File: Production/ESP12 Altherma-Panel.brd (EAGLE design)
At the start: 80.1 x 49.8 mm, 53 parts, among them CON1 PGM/BT Serial, CON2 X85A - PL, CON3 X10A, CON5 Thermo Rly, K1 HRS1KH-S_DC5V, K2 HRS1KH-S_DC5V, U1 TLP291-4, U2 AP2112K-3.3, U4 DRDC3105E6-7, U5 SN74LVC1G125GV

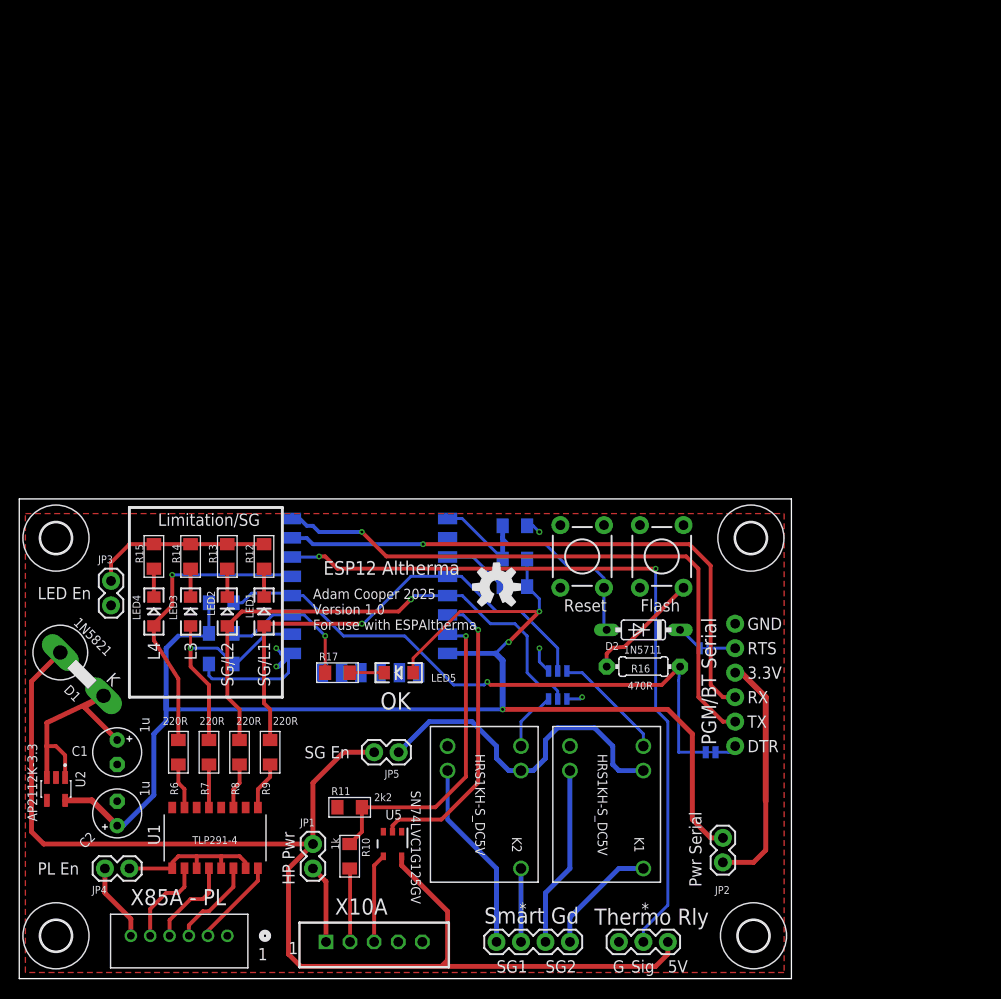
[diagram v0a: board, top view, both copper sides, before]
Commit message: Added layers 125/6 in BRD. Added panelised BRD.
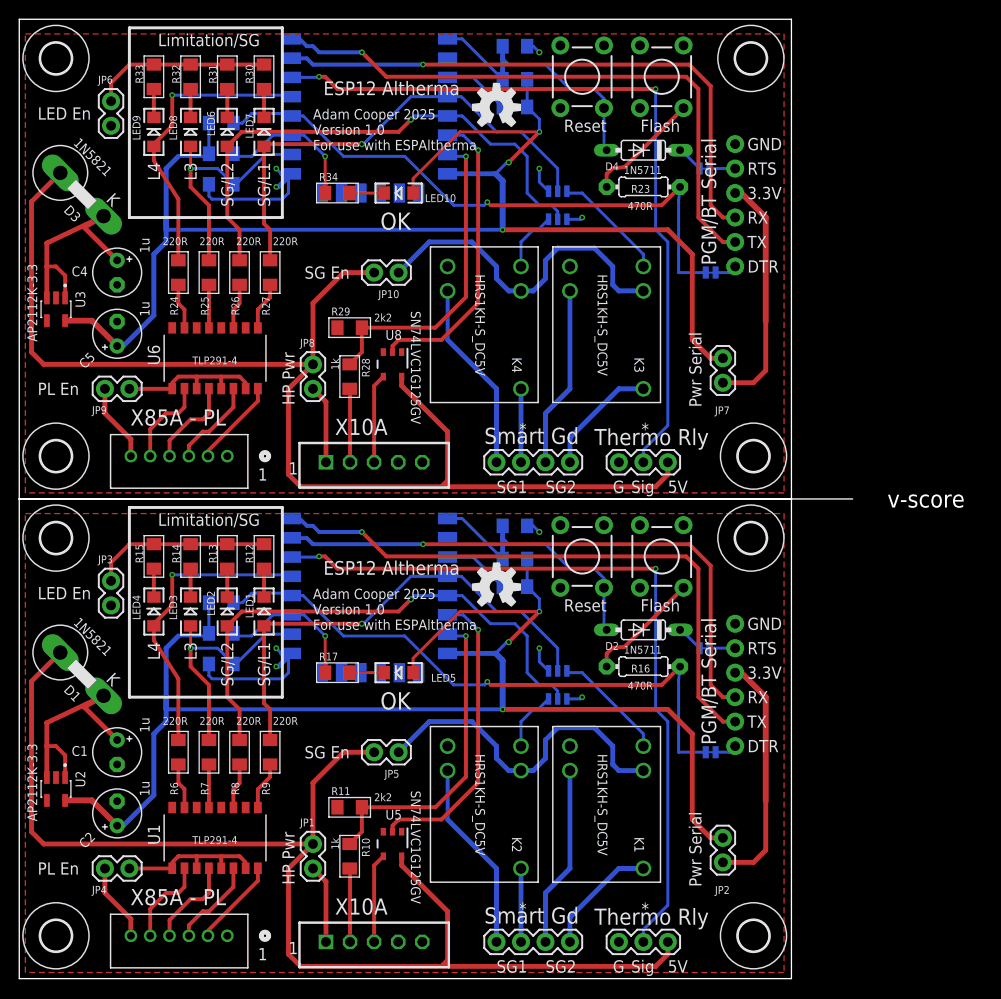
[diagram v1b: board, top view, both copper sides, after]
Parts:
- added C4, C5: 1u, Master 2016:E2,5-5
- added C6: 100n, Master 2016:1206
- added CON4: PGM/BT Serial, Master 2016:1X06-KIT
- added CON6: Thermo Rly, SparkFun-Connectors:1X03
- added CON7: X10A, con-jst-eh:B5B-EH-A
- added CON8: X85A - PL, conn-jst-pa6:CONN_B06B-PASK_JST
- added CONN1: SG, SparkFun-Connectors:1X04
- added D3: 1N5821, Master 2016:DO201-15
- added D4: 1N5711, Master 2016:DO35-7
- added H5, H6, H7, H8: MOUNT-HOLE3.2, Master 2016:3,2
- added JP10: SG En, SparkFun-Passives:1X02
- added JP6: LED En, SparkFun-Passives:1X02
- added JP7: Pwr Serial, SparkFun-Passives:1X02
- added JP8: HP Pwr, SparkFun-Passives:1X02
- added JP9: PL En, SparkFun-Passives:1X02
- added K3, K4: HRS1KH-S_DC5V, HRS1KH-S Relay:HRS1KH-S_DC5V_MTC
- added LED10, LED6, LED7, LED8, LED9: (no value), Master 2016:LED-1206
- added LOGO2: OSHW-LOGOM, Master 2016:OSHW-LOGO-M
- added R18, R19, R20, R21, R22: 10k, Master 2016:1206
- added R23: 470R, Master 2016:0204/7
- added R24, R25, R26, R27: 220R, Master 2016:1206
- added R28: 1k, Master 2016:1206
- added R29: 2k2, Master 2016:1206
- added R30, R31, R32, R33, R34: 180R, Master 2016:1206
- added S3: Reset, Master 2016:TACTILE-PTH
- added S4: Flash, Master 2016:TACTILE-PTH
- added SJ3, SJ4: SOLDERJUMPERTRACE, Master 2016:SJ_2S-TRACE
- added SJR2: (no value), esp12e:ESP8266-ESP12E0-NKE
- added U3: AP2112K-3.3, AP2112K-3.3TRG1:SOT95P285X140-5N
- added U6: TLP291-4, TLP291-4:SO16_TOS
- added U7: DRDC3105E6-7, DRDC3105E6:SOT26-DI_DIO-M
- added U8: SN74LVC1G125GV, 74LVC1G125GV:DBV0005A_L
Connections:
- new net 5V1: CON6.3, D3.A, JP10.2, JP8.1, U8.5
- new net 5V_HP1: CON7.1, JP8.2
- new net GND1: C4.-, C5.-, C6.2, CON4.1, CON6.1, CON7.5, JP6.2, R18.1, R29.1, S3.1, S4.1, SJR2.9, U3.2, U6.2, U6.4, U6.6, U6.8, U7.1, U7.4, U8.1, U8.3
- new net GPIO1: LED9.A, R24.2, SJR2.13
- new net GPIO10: R22.2, R34.1, SJR2.11
- new net GPIO11: LED7.A, R27.2, SJR2.4, U7.2
- new net GPIO17: LED8.A, R18.2, R25.2, SJR2.10
- new net GPIO3: CON6.2, SJR2.14
- new net GPIO6: SJR2.6, U8.2
- new net GPIO7: R28.1, R29.2, SJR2.7
- new net GPIO8: LED6.A, R26.2, SJR2.5, U7.5
- new net GPIO9: R19.1, R23.2, SJ3.1, SJR2.12
- new net N$30: R21.1, SJR2.3
- new net N$31: R23.1, S4.3
- new net N$32: C4.+, D3.C, U3.1, U3.3
- new net N$33: CON4.3, JP7.1
- new net N$34: CON4.6, SJ3.2
- new net N$35: CON4.2, SJ4.2
- new net N$36: D4.C, SJ4.1
- new net N$37: CON8.5, U6.10
- new net N$38: CON8.4, U6.12
- new net N$41: CON8.3, U6.14
- new net N$42: CON8.2, U6.16
- new net N$43: R24.1, U6.7
- new net N$44: R27.1, U6.1
- new net N$45: R26.1, U6.3
- new net N$46: R25.1, U6.5
- new net N$47: CON7.3, U8.4
- new net N$48: CON7.2, R28.2
- new net N$49: CONN1.1, K4.5
- new net N$50: CONN1.3, K3.5
- new net N$51: CONN1.2, K4.1
- new net N$52: CONN1.4, K3.1
- new net N$53: K3.3, U7.3
- new net N$54: K4.3, U7.6
- new net N$55: JP6.1, R30.1, R31.1, R32.1, R33.1
- new net N$56: LED8.C, R32.2
- new net N$57: LED9.C, R33.2
- new net N$58: LED7.C, R30.2
- new net N$59: LED6.C, R31.2
- new net N$60: CON8.6, JP9.1
- new net N$61: JP10.1, K3.2, K4.2
- new net N$62: LED10.C, R34.2
- new net RST1: C6.1, D4.A, R20.1, S3.3, SJR2.1
- new net RXD1: CON4.4, SJR2.15
- new net TXD1: CON4.5, SJR2.16
- new net VCC1: C5.+, JP7.2, LED10.A, R19.2, R20.2, R21.2, R22.1, SJR2.8, U3.5
- new net X85_GND1: JP9.2, U6.11, U6.13, U6.15, U6.9
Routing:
- net VCC1: track 0.00 -> 144.2 mm, vias 0 -> 3
- net 5V1: track 0.00 -> 131.4 mm
- net GPIO3: track 0.00 -> 78.8 mm, vias 0 -> 2
- net GPIO9: track 0.00 -> 63.5 mm, vias 0 -> 1
- net TXD1: track 0.00 -> 62.6 mm, vias 0 -> 1
- net RXD1: track 0.00 -> 60.1 mm, vias 0 -> 1
- net GPIO8: track 0.00 -> 55.1 mm, vias 0 -> 1
- net GPIO11: track 0.00 -> 50.2 mm, vias 0 -> 1
- net N$61: track 0.00 -> 35.5 mm
- net GPIO7: track 0.00 -> 33.0 mm, vias 0 -> 1
- net GPIO1: track 0.00 -> 31.1 mm, vias 0 -> 1
- net GPIO6: track 0.00 -> 31.1 mm, vias 0 -> 1
- net RST1: track 0.00 -> 28.6 mm
- net N$33: track 0.00 -> 25.1 mm
- net GPIO17: track 0.00 -> 25.1 mm, vias 0 -> 1
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- added copper zone on layer 1, net GND1
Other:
- board size 80.1 x 49.8 mm -> 86.5 x 99.6 mm
- board text added: "v-score"
